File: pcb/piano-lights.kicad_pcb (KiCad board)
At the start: 2 copper layers, 150 x 82 mm, 31 parts, among them J1 FTDI RS232, J2 USB_B_Micro, J3 LED Strip, J4 AVR-ISP-6, J5 MIDI IN, J6 MIDI THRU, SW1 Button, SW2 Reset, U1 ATmega328P-P, U2 H11L1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

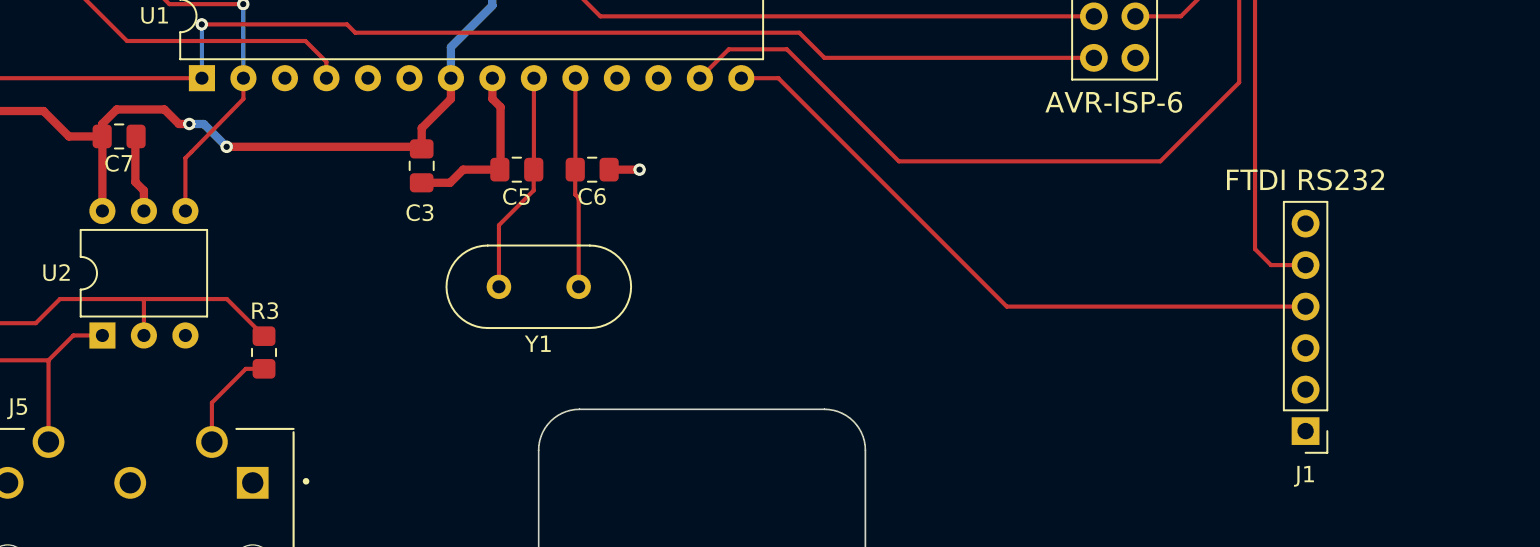
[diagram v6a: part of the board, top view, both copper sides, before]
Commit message: Update version text and date.
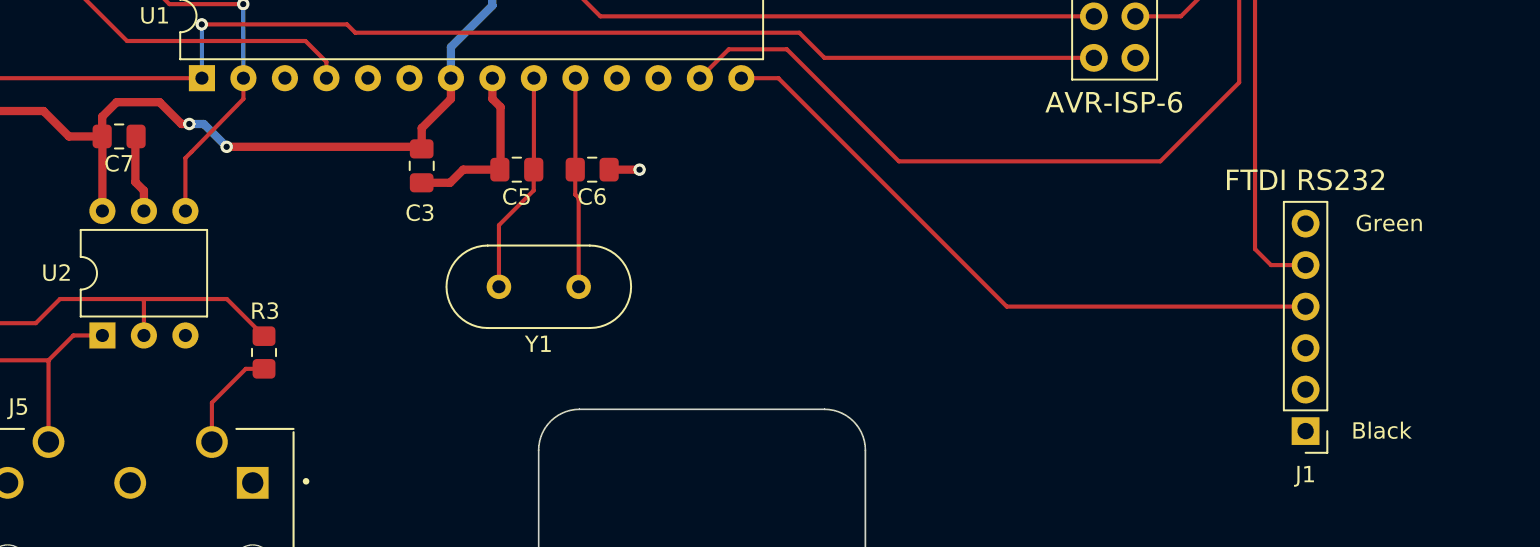
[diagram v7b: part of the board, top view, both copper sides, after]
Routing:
- net +5V: track 172.9 -> 173.5 mm
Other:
- board text added: "Black"
- board text added: "Green"
- board text added: "Piano Lights v1.0.0 Dave Dribin"
- board text removed: "Piano Lights v1.0 Dave Dribin"
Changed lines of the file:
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@@
   (title_block
     (title "Piano Lights")
-    (date "2022-05-09")
-    (rev "1.0b1")
+    (date "2022-06-26")
+    (rev "1.0.0")
     (comment 1 "Dave Dribin")
   )
@@
   (gr_arc (start 59 124) (mid 65.363961 126.636039) (end 68 133) (layer "User.2") (width 0.15))
   (gr_circle (center 65.1 69.1) (end 68.1 69.1) (layer "User.2") (width 0.15) (fill none))
-  (gr_text "Piano Lights v1.0\nDave Dribin" (at 85 114.5) (layer "B.Mask")
+  (gr_text "Green" (at 189.992 103.632) (layer "F.SilkS")
+    (effects (font (size 1 1) (thickness 0.15)) (justify left))
+  )
+  (gr_text "Black" (at 189.738 116.332) (layer "F.SilkS")
+    (effects (font (size 1 1) (thickness 0.15)) (justify left))
+  )
+  (gr_text "Piano Lights v1.0.0\nDave Dribin" (at 85 114.5) (layer "B.Mask")
     (effects (font (size 1.25 1.25) (thickness 0.2)) (justify mirror))
   )
@@
   (segment (start 115 78.4) (end 115 73.05) (width 0.508) (layer "F.Cu") (net 4))
   (segment (start 132.715 98.933) (end 132.842 99.06) (width 0.508) (layer "F.Cu") (net 4))
-  (segment (start 113.284 98.298) (end 113.284 97.536) (width 0.508) (layer "F.Cu") (net 4))
   (segment (start 132.842 97.79) (end 132.842 99.06) (width 0.508) (layer "F.Cu") (net 4))
   (segment (start 139.71 87.112) (end 139.71 85.842) (width 0.508) (layer "F.Cu") (net 4))
-  (segment (start 113.284 97.536) (end 114.173 96.647) (width 0.508) (layer "F.Cu") (net 4))
+  (segment (start 118.136 97.536) (end 118.618 97.536) (width 0.508) (layer "F.Cu") (net 4))
   (segment (start 176.5 78.8) (end 173.3 78.8) (width 0.508) (layer "F.Cu") (net 4))
   (segment (start 113.284 98.298) (end 111.252 98.298) (width 0.508) (layer "F.Cu") (net 4))
@@
   (segment (start 140.97 81) (end 142.647 81) (width 0.508) (layer "F.Cu") (net 4))
   (segment (start 121.1 60) (end 143.185 60) (width 0.508) (layer "F.Cu") (net 4))
-  (segment (start 117.983 97.536) (end 118.618 97.536) (width 0.508) (layer "F.Cu") (net 4))
   (segment (start 109.696 96.742) (end 104.394 96.742) (width 0.508) (layer "F.Cu") (net 4))
   (segment (start 115 73.05) (end 116.5 73.05) (width 0.508) (layer "F.Cu") (net 4))
@@
   (segment (start 140.97 82.03) (end 140.97 81) (width 0.508) (layer "F.Cu") (net 4))
   (segment (start 120.904 98.933) (end 132.715 98.933) (width 0.508) (layer "F.Cu") (net 4))
+  (segment (start 113.284 98.298) (end 113.284 97.089) (width 0.508) (layer "F.Cu") (net 4))
   (segment (start 142.647 81) (end 148.336 75.311) (width 0.508) (layer "F.Cu") (net 4))
   (segment (start 164.599 65.151) (end 164.75 65) (width 0.508) (layer "F.Cu") (net 4))
@@
   (segment (start 110 73.05) (end 115 73.05) (width 0.508) (layer "F.Cu") (net 4))
   (segment (start 148.336 65.151) (end 164.599 65.151) (width 0.508) (layer "F.Cu") (net 4))
+  (segment (start 113.284 97.089) (end 114.173 96.2) (width 0.508) (layer "F.Cu") (net 4))
   (segment (start 140.97 82.03) (end 140.97 81.28) (width 0.508) (layer "F.Cu") (net 4))
   (segment (start 139.71 85.842) (end 140.97 84.582) (width 0.508) (layer "F.Cu") (net 4))
   (segment (start 140.97 84.582) (end 140.97 82.03) (width 0.508) (layer "F.Cu") (net 4))
   (segment (start 134.63 96.002) (end 132.842 97.79) (width 0.508) (layer "F.Cu") (net 4))
-  (segment (start 114.173 96.647) (end 117.094 96.647) (width 0.508) (layer "F.Cu") (net 4))
   (segment (start 117.5 63.6) (end 121.1 60) (width 0.508) (layer "F.Cu") (net 4))
-  (segment (start 117.094 96.647) (end 117.983 97.536) (width 0.508) (layer "F.Cu") (net 4))
   (segment (start 140.944 81.026) (end 140.97 81) (width 0.508) (layer "F.Cu") (net 4))
   (segment (start 173.25 78.75) (end 173.3 78.8) (width 0.508) (layer "F.Cu") (net 4))
   (segment (start 116.5 73.05) (end 117.5 72.05) (width 0.508) (layer "F.Cu") (net 4))
+  (segment (start 114.173 96.2) (end 116.8 96.2) (width 0.508) (layer "F.Cu") (net 4))
   (segment (start 137.17 87.112) (end 137.17 85.862) (width 0.508) (layer "F.Cu") (net 4))
+  (segment (start 116.8 96.2) (end 118.136 97.536) (width 0.508) (layer "F.Cu") (net 4))
   (segment (start 143.185 60) (end 148.336 65.151) (width 0.508) (layer "F.Cu") (net 4))
   (segment (start 136.652 85.344) (end 136.652 81.026) (width 0.508) (layer "F.Cu") (net 4))

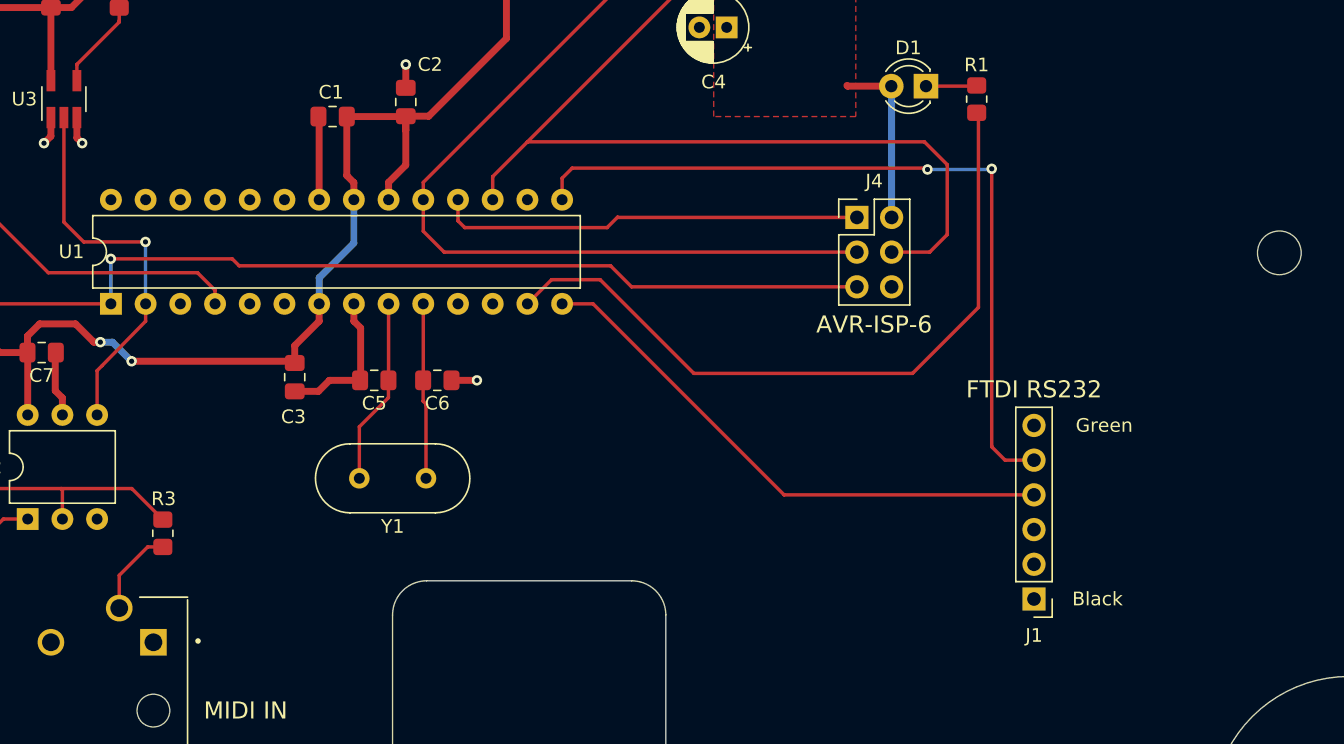
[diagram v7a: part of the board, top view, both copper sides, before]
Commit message: Add a jumper for 5V UART power. Add more silk.
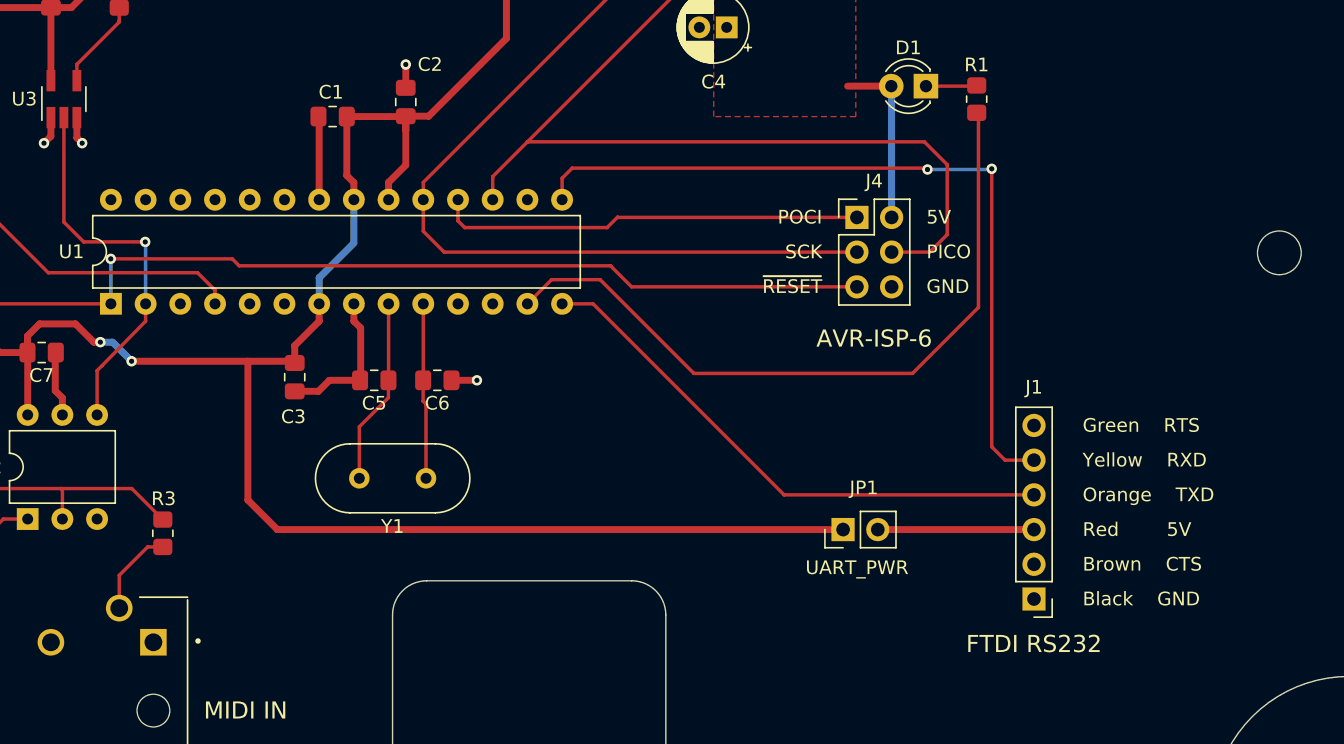
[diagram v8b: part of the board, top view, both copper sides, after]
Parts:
- added JP1: UART_PWR, Connector_PinHeader_2.54mm:PinHeader_1x02_P2.54mm_Vertical, F.Cu at (173.0, 111.3)
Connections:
- J1 pad 3: unconnected-(J1-Pad3) -> /UART_5V
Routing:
- net +5V: track 173.5 -> 228.1 mm
- net /UART_5V: track 0.00 -> 11.4 mm
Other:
- board text added: "5V"
- board text added: "Black GND"
- board text added: "Brown CTS"
- board text added: "GND"
- board text added: "Green RTS"
- board text added: "Orange TXD"
- board text added: "PICO"
- board text added: "POCI"
- board text added: "Red 5V"
- board text added: "SCK"
- board text added: "Yellow RXD"
- board text added: "~{RESET}"
- board text removed: "Black"
- board text removed: "Green"
